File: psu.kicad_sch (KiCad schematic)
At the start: 19 parts, among them J1 USB_C_Receptacle_USB2.0_16P, U2 LM1117MP-ADJ

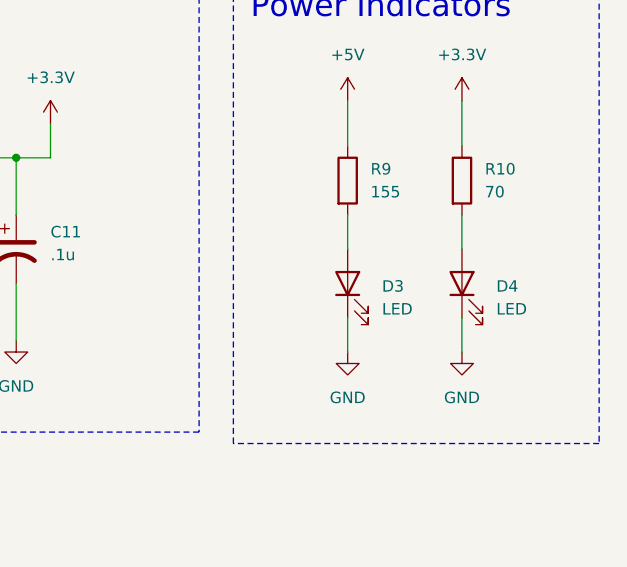
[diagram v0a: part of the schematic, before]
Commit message: delete zones for footprint editing
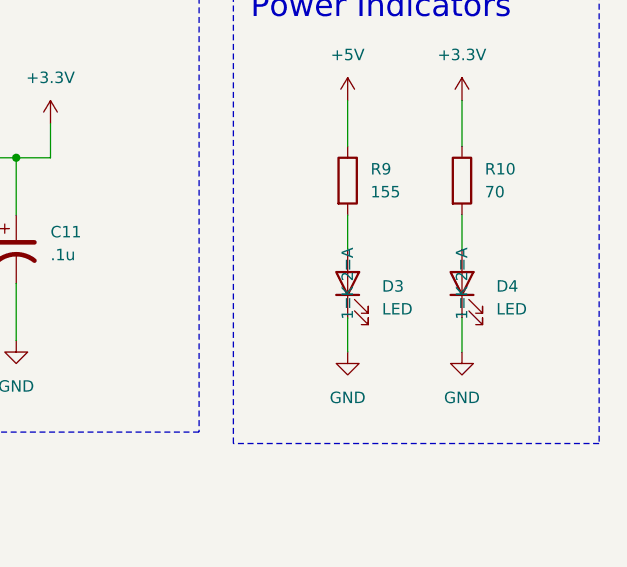
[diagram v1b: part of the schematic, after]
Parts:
- U2: footprint Package_TO_SOT_SMD:SOT-223 -> Package_TO_SOT_SMD:SOT-223-3_TabPin2
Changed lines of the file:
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@@
+			)
+		)
+		(property "Sim.Pins" "1=K 2=A"
+			(at 191.77 114.3 0)
+			(effects
+				(font
+					(size 1.27 1.27)
+				)
 			)
 		)
@@
 			)
 		)
-		(property "Footprint" "Package_TO_SOT_SMD:SOT-223"
+		(property "Footprint" "Package_TO_SOT_SMD:SOT-223-3_TabPin2"
 			(at 135.89 100.33 0)
 			(effects
@@
 			)
 		)
+		(property "Sim.Pins" "1=K 2=A"
+			(at 204.47 114.3 0)
+			(effects
+				(font
+					(size 1.27 1.27)
+				)
+			)
+		)

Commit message: routed new 0603 footprints
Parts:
- D3, D4: footprint LED_SMD:LED_0402_1005Metric -> LED_SMD:LED_0603_1608Metric
- R10, R5, R6, R7, R8, R9: footprint Resistor_SMD:R_0402_1005Metric -> Resistor_SMD:R_0603_1608Metric
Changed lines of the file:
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@@
 			)
 		)
-		(property "Footprint" "Resistor_SMD:R_0402_1005Metric"
+		(property "Footprint" "Resistor_SMD:R_0603_1608Metric"
 			(at 189.992 102.87 90)
 			(effects
@@
 			)
 		)
-		(property "Footprint" "LED_SMD:LED_0402_1005Metric"
+		(property "Footprint" "LED_SMD:LED_0603_1608Metric"
 			(at 191.77 114.3 0)
 			(effects
@@
 			)
 		)
-		(property "Footprint" "Resistor_SMD:R_0402_1005Metric"
+		(property "Footprint" "Resistor_SMD:R_0603_1608Metric"
 			(at 90.932 83.82 90)
 			(effects
@@
 			)
 		)
-		(property "Footprint" "Resistor_SMD:R_0402_1005Metric"
+		(property "Footprint" "Resistor_SMD:R_0603_1608Metric"
 			(at 202.692 102.87 90)
 			(effects
@@
 			)
 		)
-		(property "Footprint" "Resistor_SMD:R_0402_1005Metric"
+		(property "Footprint" "Resistor_SMD:R_0603_1608Metric"
 			(at 144.272 115.57 90)
 			(effects
@@
 			)
 		)
-		(property "Footprint" "LED_SMD:LED_0402_1005Metric"
+		(property "Footprint" "LED_SMD:LED_0603_1608Metric"
 			(at 204.47 114.3 0)
 			(effects
@@
 			)
 		)
-		(property "Footprint" "Resistor_SMD:R_0402_1005Metric"
+		(property "Footprint" "Resistor_SMD:R_0603_1608Metric"
 			(at 144.272 105.41 90)
 			(effects
@@
 			)
 		)
-		(property "Footprint" "Resistor_SMD:R_0402_1005Metric"
+		(property "Footprint" "Resistor_SMD:R_0603_1608Metric"
 			(at 83.312 87.63 90)
 			(effects
